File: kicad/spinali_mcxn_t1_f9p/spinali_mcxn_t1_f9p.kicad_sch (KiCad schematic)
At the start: 0 parts

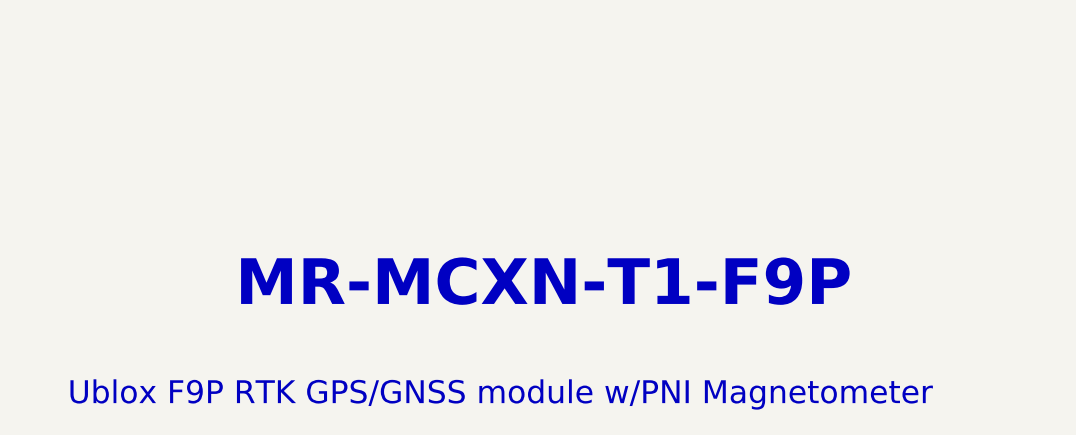
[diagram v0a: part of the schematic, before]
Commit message: Rev A production ready: schematic, layout and BOM fixes
- Rev A production ready.
- Update Resistor R10 on PCB
- Review DNP and re-add I2C pullups (no longer DNP)
- add silkscreen for revision
- Revision in title block
- add revision table
- add silkscreen for battery polarity.
- Changed 0R pull-up / pull-down resistors where possible to 10k for current protection.
- Fixed R13 footprint to correct package -> 0603 (was 0402).
- Improved BOM headers.
- Added Project text variables so Revision, Title, Designers, etc. is set automatically at multiple places.
- Updated all footprints so they match the library again (previously gave DRC error). Now 3D models also work again.
- Moved Time Pulse LED in layout to make it more visible.
- DRC succesfull.
- Added production folder in .gitignore.

Signed-off-by: Youri Tils <youri.tils@nxp.com>
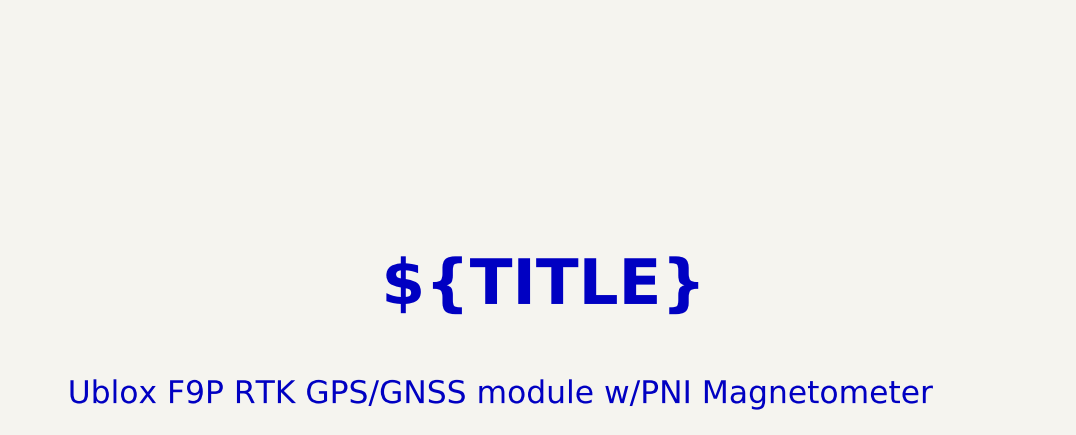
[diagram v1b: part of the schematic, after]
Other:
- company: NXP SEMICONDUCTORS B.V. -> ${COMPANY}
- title: MR-MCXN-T1-F9P -> ${TITLE}

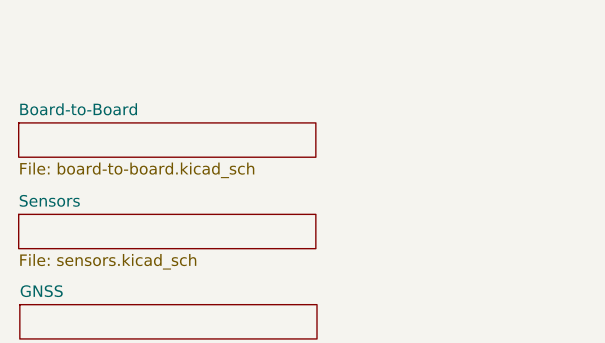
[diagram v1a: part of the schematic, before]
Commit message: add block diagram to F9P module
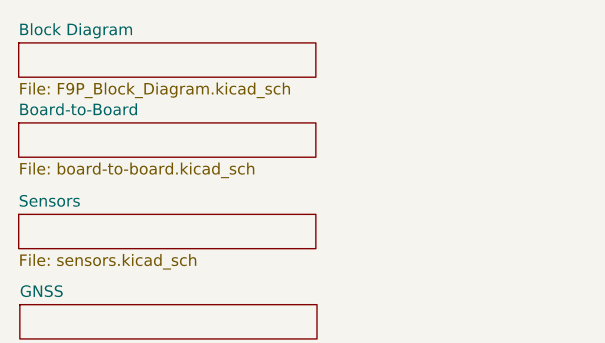
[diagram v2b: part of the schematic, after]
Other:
- added sheet Block Diagram (F9P_Block_Diagram.kicad_sch)
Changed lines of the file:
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@@
 (kicad_sch
-	(version 20250114)
+	(version 20260306)
 	(generator "eeschema")
-	(generator_version "9.0")
+	(generator_version "10.0")
 	(paper "A4")
 	(title_block
@@
 					)
 					(justify left top)
+				)
+			)
+		)
+	)
+	(sheet
+		(at 29.21 38.1)
+		(size 33.02 3.81)
+		(exclude_from_sim yes)
+		(in_bom no)
+		(on_board no)
+		(dnp no)
+		(fields_autoplaced yes)
+		(stroke
+			(width 0.1524)
+			(type solid)
+		)
+		(fill
+			(color 0 0 0 0)
+		)
+		(property "Sheetname" "Block Diagram"
+			(at 29.21 37.3884 0)
+			(show_name no)
+			(do_not_autoplace no)
+			(effects
+				(font
+					(size 1.27 1.27)
+				)
+				(justify left bottom)
+			)
+		)
+		(property "Sheetfile" "F9P_Block_Diagram.kicad_sch"
+			(at 29.21 42.4946 0)
+			(show_name no)
+			(do_not_autoplace no)
+			(effects
+				(font
+					(size 1.27 1.27)
+				)
+				(justify left top)
+			)
+		)
+		(instances
+			(project "spinali_mcxn_t1_f9p"
+				(path "/04285d74-eeba-483c-9378-52bd287e15a2"
+					(page "5")
 				)
 			)
@@
 		)
 		(fill
-			(color 0 0 0 0.0000)
+			(color 0 0 0 0)
 		)
 		(property "Sheetname" "GNSS"
 			(at 29.337 66.4714 0)
+			(show_name no)
+			(do_not_autoplace no)
 			(effects
 				(font
@@
 		(property "Sheetfile" "gnss.kicad_sch"
 			(at 29.337 71.5776 0)
+			(show_name no)
+			(do_not_autoplace no)
 			(effects
 				(font
@@
 		)
 		(fill
-			(color 0 0 0 0.0000)
+			(color 0 0 0 0)
 		)
 		(property "Sheetname" "Board-to-Board"
 			(at 29.21 46.2784 0)
+			(show_name no)
+			(do_not_autoplace no)
 			(effects
 				(font
@@
 		(property "Sheetfile" "board-to-board.kicad_sch"
 			(at 29.21 51.3846 0)
+			(show_name no)
+			(do_not_autoplace no)
 			(effects
 				(font
@@
 		)
 		(fill
-			(color 0 0 0 0.0000)
+			(color 0 0 0 0)
 		)
 		(property "Sheetname" "Sensors"
 			(at 29.21 56.4384 0)
+			(show_name no)
+			(do_not_autoplace no)
 			(effects
 				(font
@@
 		(property "Sheetfile" "sensors.kicad_sch"
 			(at 29.21 61.5446 0)
-			(effects
-				(font
+			(show_name no)
+			(do_not_autoplace no)
+			(effects
+				(font
